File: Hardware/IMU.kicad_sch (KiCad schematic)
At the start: 11 parts, among them U6 H3LIS331DLTR, U7 ICM-20608-G, U8 MMC5983MA

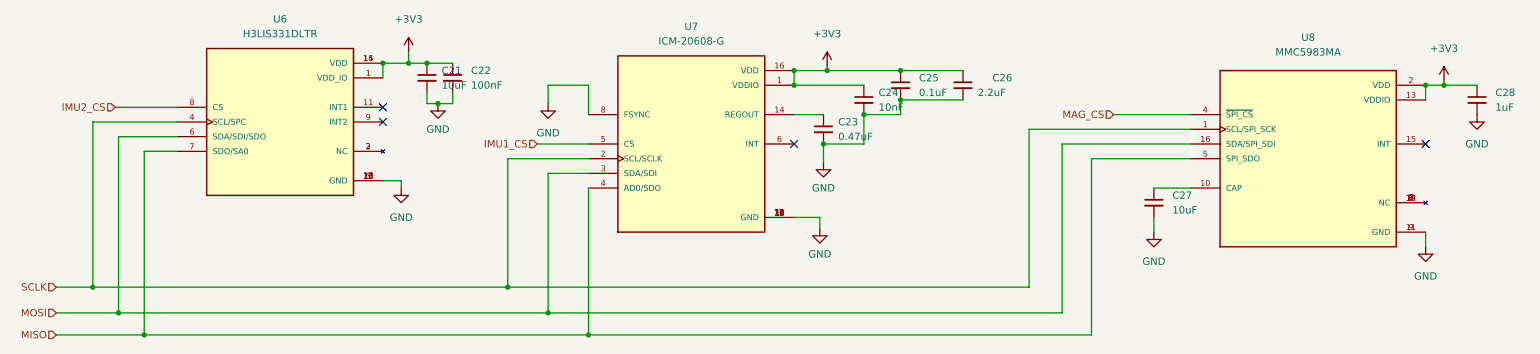
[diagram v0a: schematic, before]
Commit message: cleaned up schematic and bom
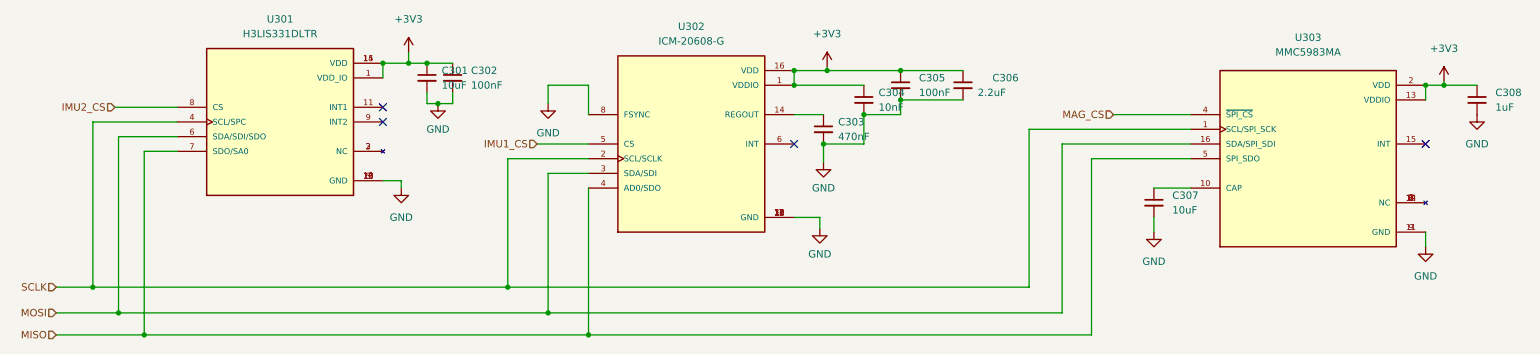
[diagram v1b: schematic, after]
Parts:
- C303: renamed from C23; value 0.47uF -> 470nF
- C305: renamed from C25; value 0.1uF -> 100nF
- renumbered C21 to C301, C22 to C302, C24 to C304, C26 to C306, C27 to C307, C28 to C308, U6 to U301, U7 to U302, U8 to U303
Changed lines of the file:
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@@
 (kicad_sch
-	(version 20231120)
+	(version 20250114)
 	(generator "eeschema")
-	(generator_version "8.0")
+	(generator_version "9.0")
 	(paper "A4")
 	(junction
@@
 		(dnp no)
 		(fields_autoplaced yes)
-		(property "Reference" "#PWR068"
+		(property "Reference" "#PWR0301"
 			(at 86.36 76.2 0)
 			(effects
@@
 			(project "PickleRick"
 				(path "/e63e39d7-6ac0-4ffd-8aa3-1841a4541b55/7b7fe22f-5db7-4fb0-a6e2-91b9a8e5f484"
-					(reference "#PWR068")
+					(reference "#PWR0301")
 					(unit 1)
 				)
@@
 		(dnp no)
 		(fields_autoplaced yes)
-		(property "Reference" "C23"
+		(property "Reference" "C303"
 			(at 161.925 58.4262 0)
 			(effects
@@
 			)
 		)
-		(property "Value" "0.47uF"
+		(property "Value" "470nF"
 			(at 161.925 60.9662 0)
 			(effects
@@
 			(project "PickleRick"
 				(path "/e63e39d7-6ac0-4ffd-8aa3-1841a4541b55/7b7fe22f-5db7-4fb0-a6e2-91b9a8e5f484"
-					(reference "C23")
+					(reference "C303")
 					(unit 1)
 				)
@@
 		(dnp no)
 		(fields_autoplaced yes)
-		(property "Reference" "#PWR078"
+		(property "Reference" "#PWR0311"
 			(at 272.415 63.5 0)
 			(effects
@@
 			(project "PickleRick"
 				(path "/e63e39d7-6ac0-4ffd-8aa3-1841a4541b55/7b7fe22f-5db7-4fb0-a6e2-91b9a8e5f484"
-					(reference "#PWR078")
+					(reference "#PWR0311")
 					(unit 1)
 				)
@@
 		(dnp no)
 		(fields_autoplaced yes)
-		(property "Reference" "#PWR076"
+		(property "Reference" "#PWR0309"
 			(at 263.525 86.36 0)
 			(effects
@@
 			(project "PickleRick"
 				(path "/e63e39d7-6ac0-4ffd-8aa3-1841a4541b55/7b7fe22f-5db7-4fb0-a6e2-91b9a8e5f484"
-					(reference "#PWR076")
+					(reference "#PWR0309")
 					(unit 1)
 				)
@@
 		(dnp no)
 		(fields_autoplaced yes)
-		(property "Reference" "C27"
+		(property "Reference" "C307"
 			(at 219.71 71.1262 0)
 			(effects
@@
 			(project "PickleRick"
 				(path "/e63e39d7-6ac0-4ffd-8aa3-1841a4541b55/7b7fe22f-5db7-4fb0-a6e2-91b9a8e5f484"
-					(reference "C27")
+					(reference "C307")
 					(unit 1)
 				)
@@
 		(dnp no)
 		(fields_autoplaced yes)
-		(property "Reference" "U7"
+		(property "Reference" "U302"
 			(at 136.525 41.91 0)
 			(effects
@@
 			)
 		)
-		(property "Datasheet" ""
+		(property "Datasheet" "https://product.tdk.com/system/files/dam/doc/product/sensor/mortion-inertial/imu/data_sheet/ds-000081-v1.01.pdf"
 			(at 136.525 62.23 0)
 			(effects
@@
 			(project "PickleRick"
 				(path "/e63e39d7-6ac0-4ffd-8aa3-1841a4541b55/7b7fe22f-5db7-4fb0-a6e2-91b9a8e5f484"
-					(reference "U7")
+					(reference "U302")
 					(unit 1)
 				)
@@
 		(dnp no)
 		(fields_autoplaced yes)
-		(property "Reference" "#PWR075"
+		(property "Reference" "#PWR0308"
 			(at 216.535 83.82 0)
 			(effects
@@
 			(project "PickleRick"
 				(path "/e63e39d7-6ac0-4ffd-8aa3-1841a4541b55/7b7fe22f-5db7-4fb0-a6e2-91b9a8e5f484"
-					(reference "#PWR075")
+					(reference "#PWR0308")
 					(unit 1)
 				)
@@
 		(dnp no)
 		(fields_autoplaced yes)
-		(property "Reference" "#PWR074"
+		(property "Reference" "#PWR0307"
 			(at 160.02 52.705 0)
 			(effects
@@
 			(project "PickleRick"
 				(path "/e63e39d7-6ac0-4ffd-8aa3-1841a4541b55/7b7fe22f-5db7-4fb0-a6e2-91b9a8e5f484"
-					(reference "#PWR074")
+					(reference "#PWR0307")
 					(unit 1)
 				)
@@
 		(dnp no)
 		(fields_autoplaced yes)
-		(property "Reference" "C28"
+		(property "Reference" "C308"
 			(at 275.59 53.3462 0)
 			(effects
@@
 			(project "PickleRick"
 				(path "/e63e39d7-6ac0-4ffd-8aa3-1841a4541b55/7b7fe22f-5db7-4fb0-a6e2-91b9a8e5f484"
-					(reference "C28")
+					(reference "C308")
 					(unit 1)
 				)
@@
 		(dnp no)
 		(fields_autoplaced yes)
-		(property "Reference" "#PWR069"
+		(property "Reference" "#PWR0302"
 			(at 87.63 50.165 0)
 			(effects
@@
 			(project "PickleRick"
 				(path "/e63e39d7-6ac0-4ffd-8aa3-1841a4541b55/7b7fe22f-5db7-4fb0-a6e2-91b9a8e5f484"
-					(reference "#PWR069")
+					(reference "#PWR0302")
 					(unit 1)
 				)
@@
 		(dnp no)
 		(fields_autoplaced yes)
-		(property "Reference" "#PWR070"
+		(property "Reference" "#PWR0303"
 			(at 92.71 61.595 0)
 			(effects
@@
 			(project "PickleRick"
 				(path "/e63e39d7-6ac0-4ffd-8aa3-1841a4541b55/7b7fe22f-5db7-4fb0-a6e2-91b9a8e5f484"
-					(reference "#PWR070")
+					(reference "#PWR0303")
 					(unit 1)
 				)
@@
 		(dnp no)
 		(fields_autoplaced yes)
-		(property "Reference" "#PWR073"
+		(property "Reference" "#PWR0306"
 			(at 159.385 71.755 0)
 			(effects
@@
 			(project "PickleRick"
 				(path "/e63e39d7-6ac0-4ffd-8aa3-1841a4541b55/7b7fe22f-5db7-4fb0-a6e2-91b9a8e5f484"
-					(reference "#PWR073")
+					(reference "#PWR0306")
 					(unit 1)
 				)
@@
 		(dnp no)
 		(fields_autoplaced yes)
-		(property "Reference" "#PWR072"
+		(property "Reference" "#PWR0305"
 			(at 158.75 83.185 0)
 			(effects
@@
 			(project "PickleRick"
 				(path "/e63e39d7-6ac0-4ffd-8aa3-1841a4541b55/7b7fe22f-5db7-4fb0-a6e2-91b9a8e5f484"
-					(reference "#PWR072")
+					(reference "#PWR0305")
 					(unit 1)
 				)
@@
 		(dnp no)
 		(fields_autoplaced yes)
-		(property "Reference" "C25"
+		(property "Reference" "C305"
 			(at 175.895 50.8062 0)
 			(effects
@@
 			)
 		)
-		(property "Value" "0.1uF"
+		(property "Value" "100nF"
 			(at 175.895 53.3462 0)
 			(effects
@@
 			(project "PickleRick"
 				(path "/e63e39d7-6ac0-4ffd-8aa3-1841a4541b55/7b7fe22f-5db7-4fb0-a6e2-91b9a8e5f484"
-					(reference "C25")
+					(reference "C305")
 					(unit 1)
 				)
@@
 		(dnp no)
 		(fields_autoplaced yes)
-		(property "Reference" "C21"
+		(property "Reference" "C301"
 			(at 93.345 49.5362 0)
 			(effects
@@
 			(project "PickleRick"
 				(path "/e63e39d7-6ac0-4ffd-8aa3-1841a4541b55/7b7fe22f-5db7-4fb0-a6e2-91b9a8e5f484"
-					(reference "C21")
+					(reference "C301")
 					(unit 1)
 				)
@@
 		(dnp no)
 		(fields_autoplaced yes)
-		(property "Reference" "#PWR077"
+		(property "Reference" "#PWR0310"
 			(at 266.7 55.245 0)
 			(effects
@@
 			(project "PickleRick"
 				(path "/e63e39d7-6ac0-4ffd-8aa3-1841a4541b55/7b7fe22f-5db7-4fb0-a6e2-91b9a8e5f484"
-					(reference "#PWR077")
+					(reference "#PWR0310")
 					(unit 1)
 				)
@@
 		(dnp no)
 		(fields_autoplaced yes)
-		(property "Reference" "U6"
+		(property "Reference" "U301"
 			(at 65.405 40.64 0)
 			(effects
@@
 			)
 		)
-		(property "Datasheet" ""
+		(property "Datasheet" "https://www.st.com/resource/en/datasheet/h3lis331dl.pdf"
 			(at 65.405 58.42 0)
 			(effects
@@
 			(project "PickleRick"
 				(path "/e63e39d7-6ac0-4ffd-8aa3-1841a4541b55/7b7fe22f-5db7-4fb0-a6e2-91b9a8e5f484"
-					(reference "U6")
+					(reference "U301")
 					(unit 1)
 				)
@@
 		(dnp no)
 		(fields_autoplaced yes)
-		(property "Reference" "C22"
+		(property "Reference" "C302"
 			(at 98.425 49.5362 0)
 			(effects
@@
 			(project "PickleRick"
 				(path "/e63e39d7-6ac0-4ffd-8aa3-1841a4541b55/7b7fe22f-5db7-4fb0-a6e2-91b9a8e5f484"
-					(reference "C22")
+					(reference "C302")
 					(unit 1)
 				)
@@
 		(dnp no)
 		(fields_autoplaced yes)
-		(property "Reference" "U8"
+		(property "Reference" "U303"
 			(at 243.205 43.815 0)
 			(effects
@@
 			)
 		)
-		(property "Datasheet" ""
+		(property "Datasheet" "https://www.mouser.com/catalog/specsheets/Memsic_09102019_MMC5983MA%20Datasheet%20Rev%20A.pdf"
 			(at 243.205 64.77 0)
 			(effects
@@
 			(project "PickleRick"
 				(path "/e63e39d7-6ac0-4ffd-8aa3-1841a4541b55/7b7fe22f-5db7-4fb0-a6e2-91b9a8e5f484"
-					(reference "U8")
+					(reference "U303")
 					(unit 1)
 				)
@@
 		(on_board yes)
 		(dnp no)
-		(property "Reference" "C26"
+		(property "Reference" "C306"
 			(at 188.595 50.8 0)
 			(effects
@@
 			(project "PickleRick"
 				(path "/e63e39d7-6ac0-4ffd-8aa3-1841a4541b55/7b7fe22f-5db7-4fb0-a6e2-91b9a8e5f484"
-					(reference "C26")
+					(reference "C306")
 					(unit 1)
 				)
@@
 		(dnp no)
 		(fields_autoplaced yes)
-		(property "Reference" "C24"
+		(property "Reference" "C304"
 			(at 168.91 53.3462 0)
 			(effects
@@
 			(project "PickleRick"
 				(path "/e63e39d7-6ac0-4ffd-8aa3-1841a4541b55/7b7fe22f-5db7-4fb0-a6e2-91b9a8e5f484"
-					(reference "C24")
+					(reference "C304")
 					(unit 1)
 				)
@@
 		(dnp no)
 		(fields_autoplaced yes)
-		(property "Reference" "#PWR071"
+		(property "Reference" "#PWR0304"
 			(at 111.76 61.595 0)
 			(effects
@@
 			(project "PickleRick"
 				(path "/e63e39d7-6ac0-4ffd-8aa3-1841a4541b55/7b7fe22f-5db7-4fb0-a6e2-91b9a8e5f484"
-					(reference "#PWR071")
+					(reference "#PWR0304")
 					(unit 1)
 				)
